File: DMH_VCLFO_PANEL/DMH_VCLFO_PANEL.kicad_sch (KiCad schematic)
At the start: 47 parts, among them J0 Panel_GND_Solder_Wire_Pad

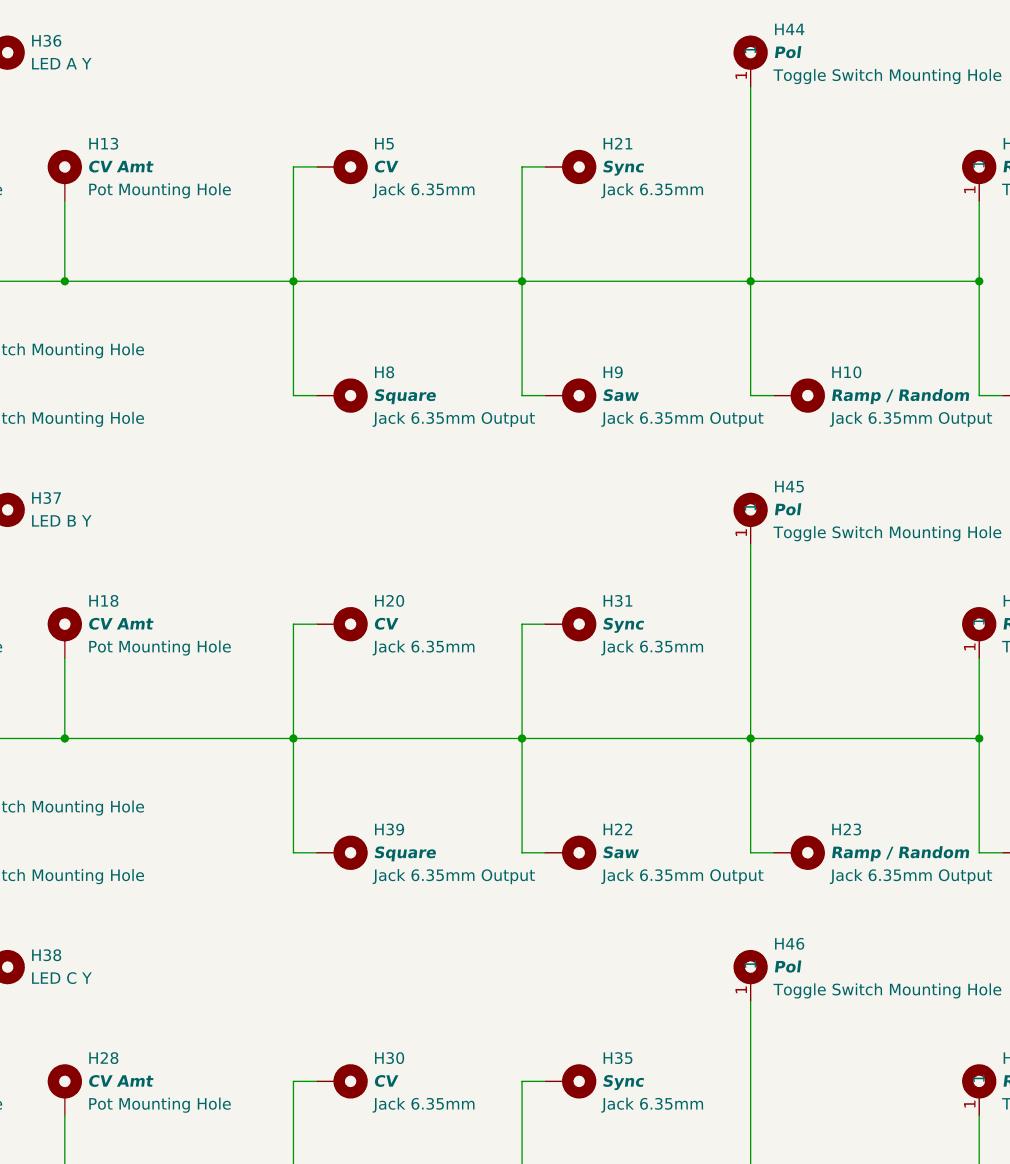
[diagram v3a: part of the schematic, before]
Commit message: Modified front panel
Added V/Oct calib trimpot hole
Replaced Polarity switch with Bus CV
Added Fine as normalized function of CV Amt pot
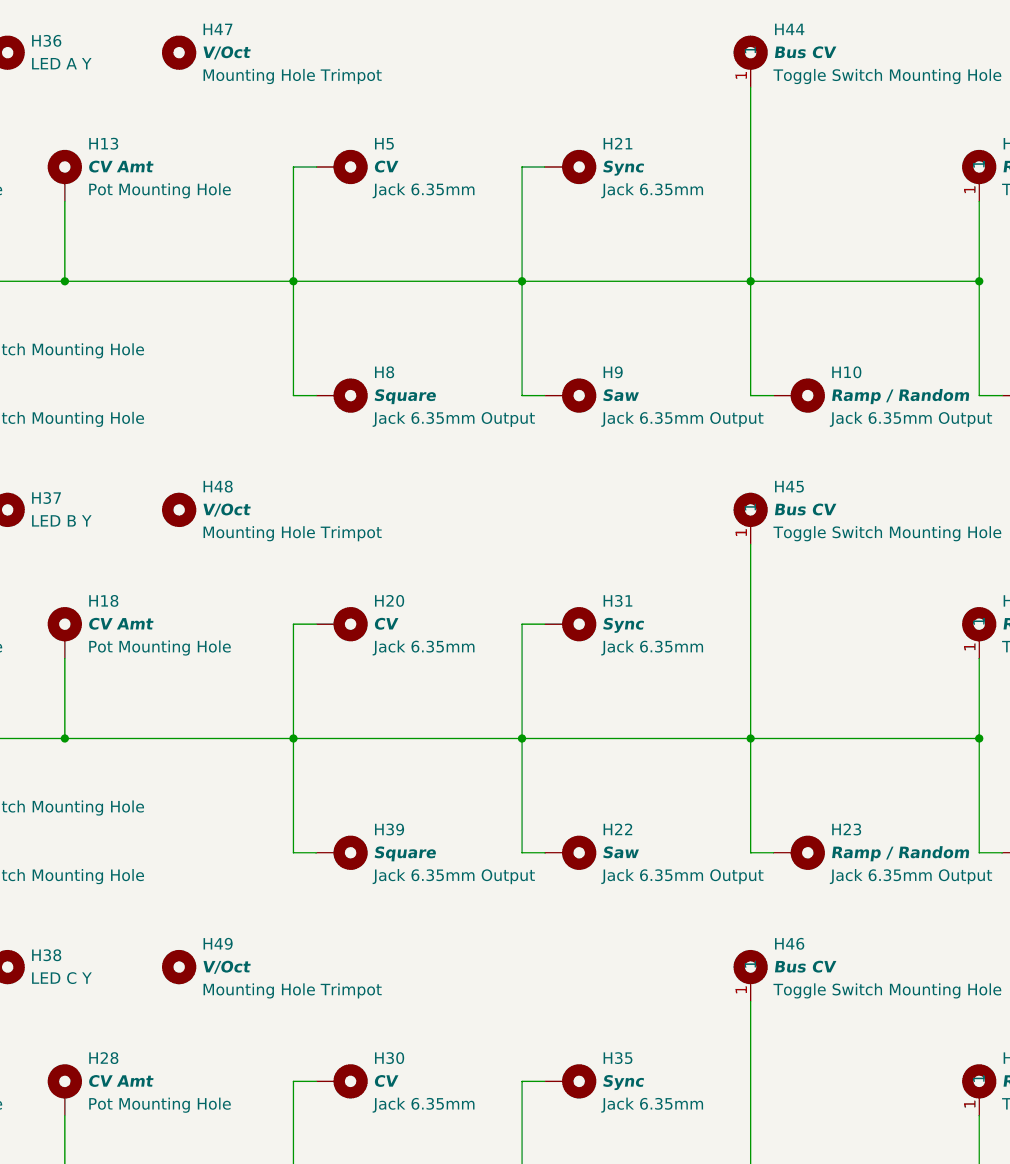
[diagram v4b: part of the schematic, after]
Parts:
- added H47, H48, H49: V/Oct, SynthStuff:MountingHole_TrimPot, symbol SynthStuff:MountingHole_Trimpot
- H13, H18, H28: footprint SynthStuff:Pot_Cutout_Tiny_attv_P110KH1 -> SynthStuff:Pot_Cutout_Tiny_attv_RD901F
- H44, H45, H46: value Pol -> Bus CV
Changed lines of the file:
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@@
 			)
 		)
-		(property "Footprint" "SynthStuff:Pot_Cutout_Tiny_attv_P110KH1"
+		(property "Footprint" "SynthStuff:Pot_Cutout_Tiny_attv_RD901F"
 			(at 57.15 102.87 0)
 			(effects
@@
 			)
 		)
-		(property "Footprint" "SynthStuff:Pot_Cutout_Tiny_attv_P110KH1"
+		(property "Footprint" "SynthStuff:Pot_Cutout_Tiny_attv_RD901F"
 			(at 57.15 153.67 0)
 			(effects
@@
 			)
 		)
-		(property "Value" "Pol"
+		(property "Value" "Bus CV"
 			(at 135.89 88.9 0)
 			(effects
@@
 	)
 	(symbol
+		(lib_id "SynthStuff:MountingHole_Trimpot")
+		(at 69.85 139.7 0)
+		(unit 1)
+		(exclude_from_sim no)
+		(in_bom no)
+		(on_board yes)
+		(dnp no)
+		(fields_autoplaced yes)
+		(property "Reference" "H49"
+			(at 72.39 137.1599 0)
+			(effects
+				(font
+					(size 1.27 1.27)
+				)
+				(justify left)
+			)
+		)
+		(property "Value" "V/Oct"
+			(at 72.39 139.7 0)
+			(effects
+				(font
+					(size 1.27 1.27)
+					(thickness 0.254)
+					(bold yes)
+					(italic yes)
+				)
+				(justify left)
+			)
+		)
+		(property "Footprint" "SynthStuff:MountingHole_TrimPot"
+			(at 69.85 139.7 0)
+			(effects
+				(font
+					(size 1.27 1.27)
+				)
+				(hide yes)
+			)
+		)
+		(property "Datasheet" "~"
+			(at 69.85 139.7 0)
+			(effects
+				(font
+					(size 1.27 1.27)
+				)
+				(hide yes)
+			)
+		)
+		(property "Description" "Mounting Hole Trimpot"
+			(at 72.39 142.2399 0)
+			(effects
+				(font
+					(size 1.27 1.27)
+				)
+				(justify left)
+			)
+		)
+		(instances
+			(project "DMH_VCLFO_PANEL"
+				(path "/a552705f-a9fe-462e-9913-5cfcc08b233c"
+					(reference "H49")
+					(unit 1)
+				)
+			)
+		)
+	)
+	(symbol
 		(lib_id "Mechanical:MountingHole")
 		(at 31.75 38.1 0)
@@
 			)
 		)
-		(property "Value" "Pol"
+		(property "Value" "Bus CV"
 			(at 135.89 139.7 0)
 			(effects
@@
 	)
 	(symbol
+		(lib_id "SynthStuff:MountingHole_Trimpot")
+		(at 69.85 38.1 0)
+		(unit 1)
+		(exclude_from_sim no)
+		(in_bom no)
+		(on_board yes)
+		(dnp no)
+		(fields_autoplaced yes)
+		(property "Reference" "H47"
+			(at 72.39 35.5599 0)
+			(effects
+				(font
+					(size 1.27 1.27)
+				)
+				(justify left)
+			)
+		)
+		(property "Value" "V/Oct"
+			(at 72.39 38.1 0)
+			(effects
+				(font
+					(size 1.27 1.27)
+					(thickness 0.254)
+					(bold yes)
+					(italic yes)
+				)
+				(justify left)
+			)
+		)
+		(property "Footprint" "SynthStuff:MountingHole_TrimPot"
+			(at 69.85 38.1 0)
+			(effects
+				(font
+					(size 1.27 1.27)
+				)
+				(hide yes)
+			)
+		)
+		(property "Datasheet" "~"
+			(at 69.85 38.1 0)
+			(effects
+				(font
+					(size 1.27 1.27)
+				)
+				(hide yes)
+			)
+		)
+		(property "Description" "Mounting Hole Trimpot"
+			(at 72.39 40.6399 0)
+			(effects
+				(font
+					(size 1.27 1.27)
+				)
+				(justify left)
+			)
+		)
+		(instances
+			(project ""
+				(path "/a552705f-a9fe-462e-9913-5cfcc08b233c"
+					(reference "H47")
+					(unit 1)
+				)
+			)
+		)
+	)
+	(symbol
 		(lib_id "SynthStuff:MountingHole_Jack6.35mm_Output_v2")
 		(at 114.3 177.8 0)
@@
 			)
 		)
-		(property "Value" "Pol"
+		(property "Value" "Bus CV"
 			(at 135.89 38.1 0)
 			(effects
@@
 	)
 	(symbol
+		(lib_id "SynthStuff:MountingHole_Trimpot")
+		(at 69.85 88.9 0)
+		(unit 1)
+		(exclude_from_sim no)
+		(in_bom no)
+		(on_board yes)
+		(dnp no)
+		(fields_autoplaced yes)
+		(property "Reference" "H48"
+			(at 72.39 86.3599 0)
+			(effects
+				(font
+					(size 1.27 1.27)
+				)
+				(justify left)
+			)
+		)
+		(property "Value" "V/Oct"
+			(at 72.39 88.9 0)
+			(effects
+				(font
+					(size 1.27 1.27)
+					(thickness 0.254)
+					(bold yes)
+					(italic yes)
+				)
+				(justify left)
+			)
+		)
+		(property "Footprint" "SynthStuff:MountingHole_TrimPot"
+			(at 69.85 88.9 0)
+			(effects
+				(font
+					(size 1.27 1.27)
+				)
+				(hide yes)
+			)
+		)
+		(property "Datasheet" "~"
+			(at 69.85 88.9 0)
+			(effects
+				(font
+					(size 1.27 1.27)
+				)
+				(hide yes)
+			)
+		)
+		(property "Description" "Mounting Hole Trimpot"
+			(at 72.39 91.4399 0)
+			(effects
+				(font
+					(size 1.27 1.27)
+				)
+				(justify left)
+			)
+		)
+		(instances
+			(project "DMH_VCLFO_PANEL"
+				(path "/a552705f-a9fe-462e-9913-5cfcc08b233c"
+					(reference "H48")
+					(unit 1)
+				)
+			)
+		)
+	)
+	(symbol
 		(lib_id "SynthStuff:MountingHole_Jack6.35mm_v2")
 		(at 114.3 152.4 0)
@@
 			)
 		)
-		(property "Footprint" "SynthStuff:Pot_Cutout_Tiny_attv_P110KH1"
+		(property "Footprint" "SynthStuff:Pot_Cutout_Tiny_attv_RD901F"
 			(at 57.15 52.07 0)
 			(effects

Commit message: Sch redesign in progress
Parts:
- added H50, H51, H52: Fine Rng, SynthStuff:MountingHole_TrimPot, symbol SynthStuff:MountingHole_Trimpot
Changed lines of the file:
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@@
+	(symbol
+		(lib_id "SynthStuff:MountingHole_Trimpot")
+		(at 101.6 38.1 0)
+		(unit 1)
+		(exclude_from_sim no)
+		(in_bom no)
+		(on_board yes)
+		(dnp no)
+		(fields_autoplaced yes)
+		(property "Reference" "H50"
+			(at 104.14 35.5599 0)
+			(effects
+				(font
+					(size 1.27 1.27)
+				)
+				(justify left)
+			)
+		)
+		(property "Value" "Fine Rng"
+			(at 104.14 38.1 0)
+			(effects
+				(font
+					(size 1.27 1.27)
+					(thickness 0.254)
+					(bold yes)
+					(italic yes)
+				)
+				(justify left)
+			)
+		)
+		(property "Footprint" "SynthStuff:MountingHole_TrimPot"
+			(at 101.6 38.1 0)
+			(effects
+				(font
+					(size 1.27 1.27)
+				)
+				(hide yes)
+			)
+		)
+		(property "Datasheet" "~"
+			(at 101.6 38.1 0)
+			(effects
+				(font
+					(size 1.27 1.27)
+				)
+				(hide yes)
+			)
+		)
+		(property "Description" "Mounting Hole Trimpot"
+			(at 104.14 40.6399 0)
+			(effects
+				(font
+					(size 1.27 1.27)
+				)
+				(justify left)
+			)
+		)
+		(instances
+			(project "DMH_VCLFO_PANEL"
+				(path "/a552705f-a9fe-462e-9913-5cfcc08b233c"
+					(reference "H50")
+					(unit 1)
+				)
+			)
+		)
+	)
 	(symbol
 		(lib_id "SynthStuff:MountingHole_Trimpot")
@@
 	)
 	(symbol
+		(lib_id "SynthStuff:MountingHole_Trimpot")
+		(at 101.6 139.7 0)
+		(unit 1)
+		(exclude_from_sim no)
+		(in_bom no)
+		(on_board yes)
+		(dnp no)
+		(fields_autoplaced yes)
+		(property "Reference" "H52"
+			(at 104.14 137.1599 0)
+			(effects
+				(font
+					(size 1.27 1.27)
+				)
+				(justify left)
+			)
+		)
+		(property "Value" "Fine Rng"
+			(at 104.14 139.7 0)
+			(effects
+				(font
+					(size 1.27 1.27)
+					(thickness 0.254)
+					(bold yes)
+					(italic yes)
+				)
+				(justify left)
+			)
+		)
+		(property "Footprint" "SynthStuff:MountingHole_TrimPot"
+			(at 101.6 139.7 0)
+			(effects
+				(font
+					(size 1.27 1.27)
+				)
+				(hide yes)
+			)
+		)
+		(property "Datasheet" "~"
+			(at 101.6 139.7 0)
+			(effects
+				(font
+					(size 1.27 1.27)
+				)
+				(hide yes)
+			)
+		)
+		(property "Description" "Mounting Hole Trimpot"
+			(at 104.14 142.2399 0)
+			(effects
+				(font
+					(size 1.27 1.27)
+				)
+				(justify left)
+			)
+		)
+		(instances
+			(project "DMH_VCLFO_PANEL"
+				(path "/a552705f-a9fe-462e-9913-5cfcc08b233c"
+					(reference "H52")
+					(unit 1)
+				)
+			)
+		)
+	)
+	(symbol
 		(lib_id "SynthStuff:MountingHole_Jack6.35mm_Output_v2")
 		(at 114.3 177.8 0)
@@
 					(unit 1)
 				)
+			)
+		)
+	)
+	(symbol
+		(lib_id "SynthStuff:MountingHole_Trimpot")
+		(at 101.6 88.9 0)
+		(unit 1)
+		(exclude_from_sim no)
+		(in_bom no)
+		(on_board yes)
+		(dnp no)
+		(fields_autoplaced yes)
+		(property "Reference" "H51"
+			(at 104.14 86.3599 0)
+			(effects
+				(font
+					(size 1.27 1.27)
+				)
+				(justify left)
+			)
+		)
+		(property "Value" "Fine Rng"
+			(at 104.14 88.9 0)
+			(effects
+				(font
+					(size 1.27 1.27)
+					(thickness 0.254)
+					(bold yes)
+					(italic yes)
+				)
+				(justify left)
+			)
+		)
+		(property "Footprint" "SynthStuff:MountingHole_TrimPot"
+			(at 101.6 88.9 0)
+			(effects
+				(font
+					(size 1.27 1.27)
+				)
+				(hide yes)
+			)
+		)
+		(property "Datasheet" "~"
+			(at 101.6 88.9 0)
+			(effects
+				(font
+					(size 1.27 1.27)
+				)
+				(hide yes)
+			)
+		)
+		(property "Description" "Mounting Hole Trimpot"
+			(at 104.14 91.4399 0)
+			(effects
+				(font
+					(size 1.27 1.27)
+				)
+				(justify left)
+			)
+		)
+		(instances
+			(project "DMH_VCLFO_PANEL"
+				(path "/a552705f-a9fe-462e-9913-5cfcc08b233c"
+					(reference "H51")
+					(unit 1)
+				)
